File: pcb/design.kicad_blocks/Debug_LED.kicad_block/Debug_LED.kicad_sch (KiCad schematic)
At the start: 4 parts

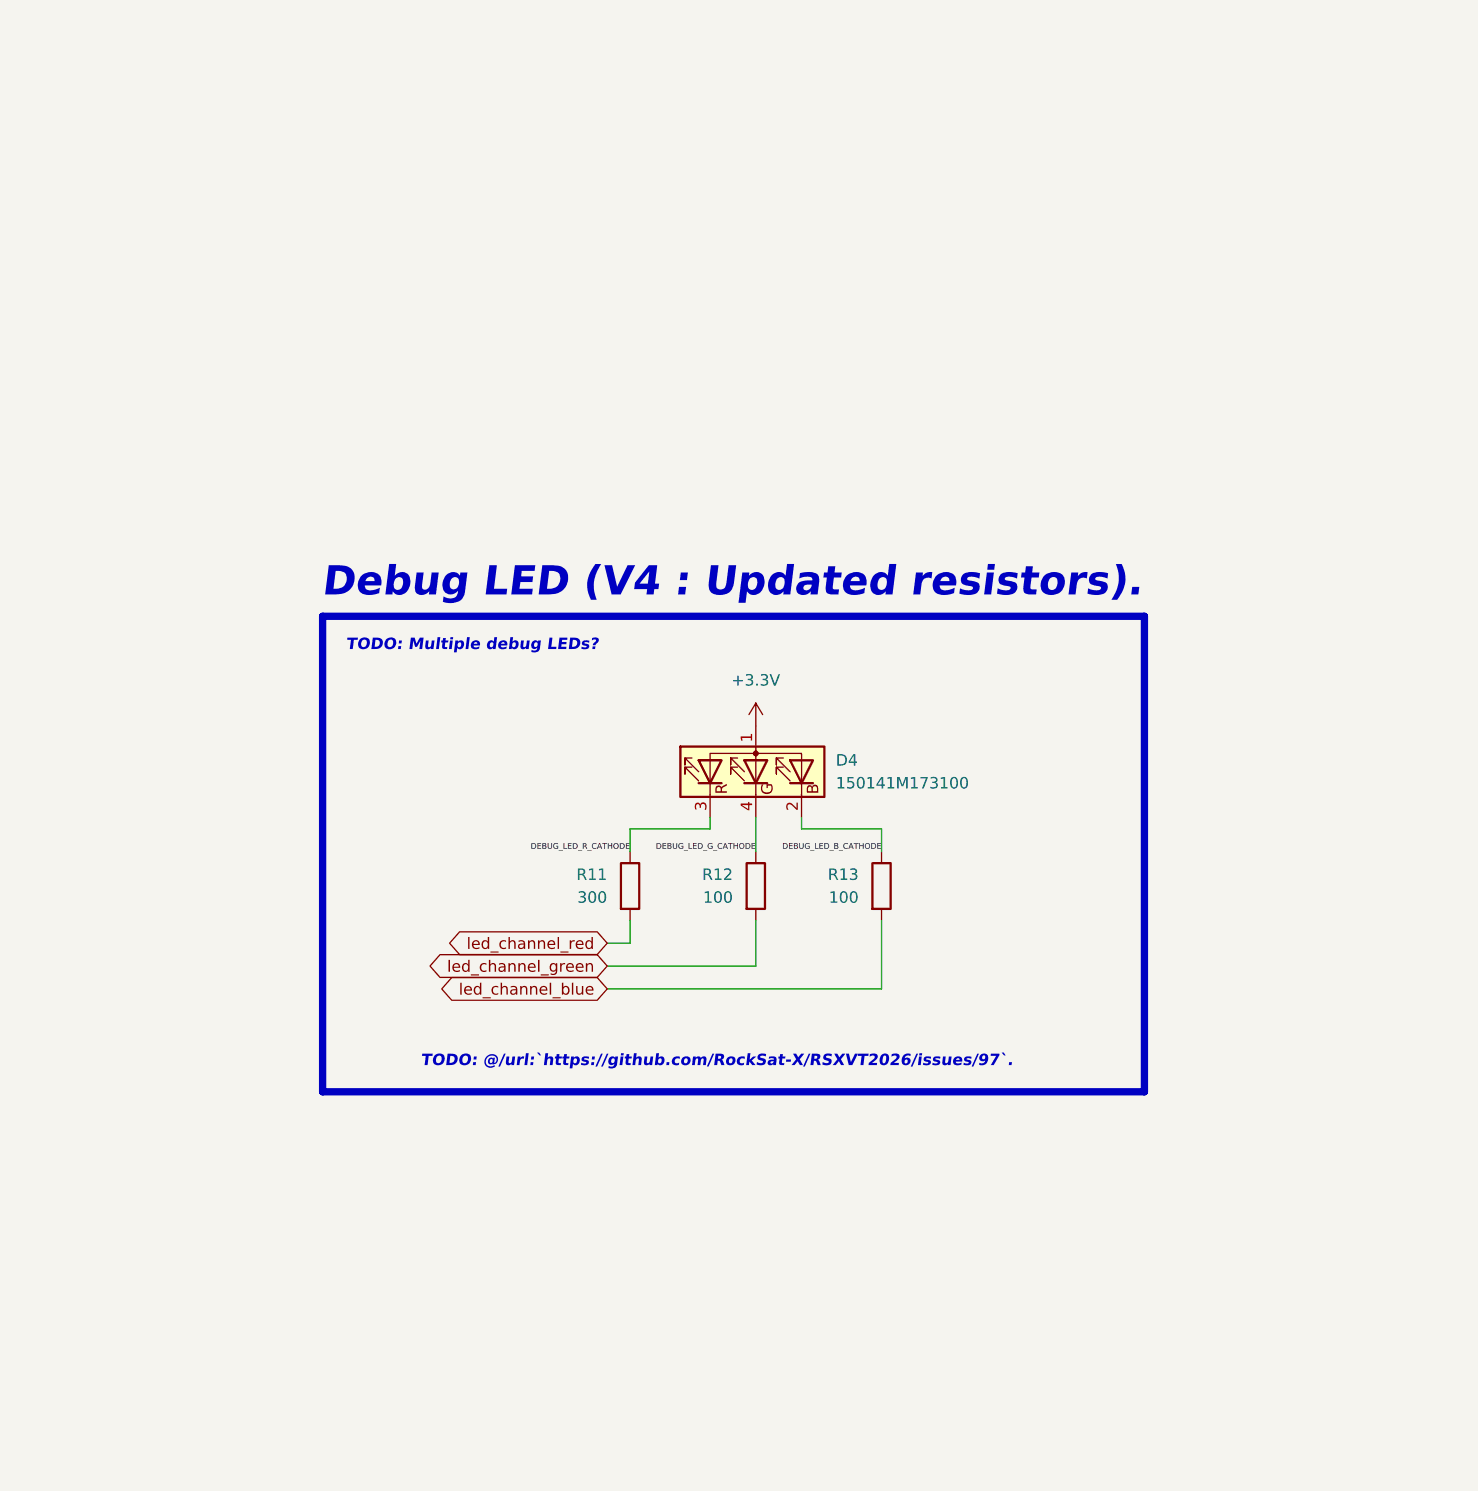
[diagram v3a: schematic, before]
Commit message: `Debug LED (V5 : Removed local nets).`
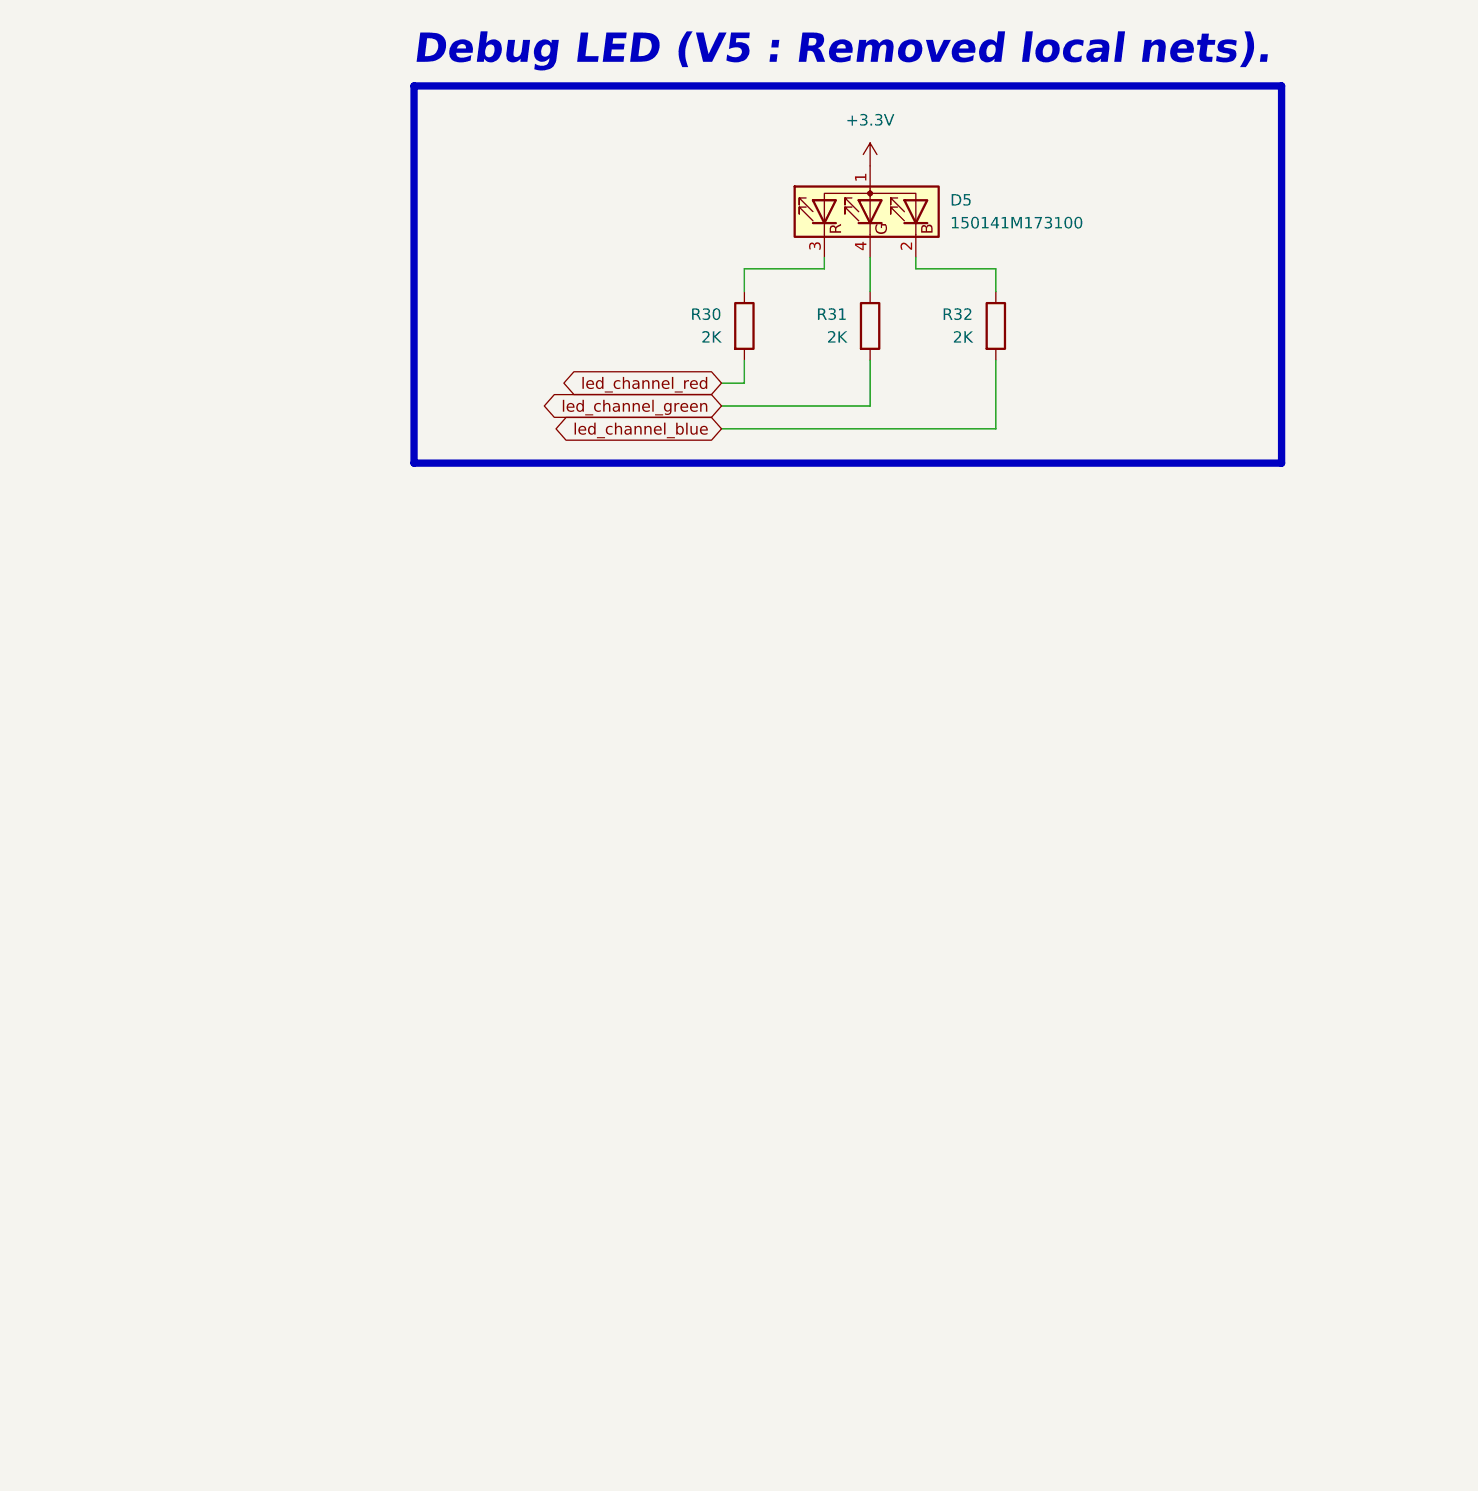
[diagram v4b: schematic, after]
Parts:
- R30: renamed from R11; value 300 -> 2K
- R31: renamed from R12; value 100 -> 2K
- R32: renamed from R13; value 100 -> 2K
- renumbered D4 to D5
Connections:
- net DEBUG_LED_B_CATHODE: no longer names the net of D5.2 (BK), R32.1
- net DEBUG_LED_G_CATHODE: no longer names the net of D5.4 (GK), R31.1
- net DEBUG_LED_R_CATHODE: no longer names the net of D5.3 (RK), R30.1
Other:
- note added: "Debug LED (V5 : Removed local nets)."
- note removed: "Debug LED (V4 : Updated resistors)."
- note removed: "TODO: @/url:`https://github.com/RockSat-X/RSXVT2026/issues/97`."
- note removed: "TODO: Multiple debug LEDs?"
- moved on the sheet: D5, R30, R31, R32
